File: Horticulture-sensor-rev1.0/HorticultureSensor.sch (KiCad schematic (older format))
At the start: 24 parts, among them J1 Conn_01x04, J2 Conn_02x05_Odd_Even, J3 Conn_01x03, J4 Conn_01x04, J5 Conn_01x03, J6 Conn_01x02, J7 Conn_01x02, J8 Conn_01x02, Q1 IRLML2030TRPBF, Q2 IRLML2030TRPBF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

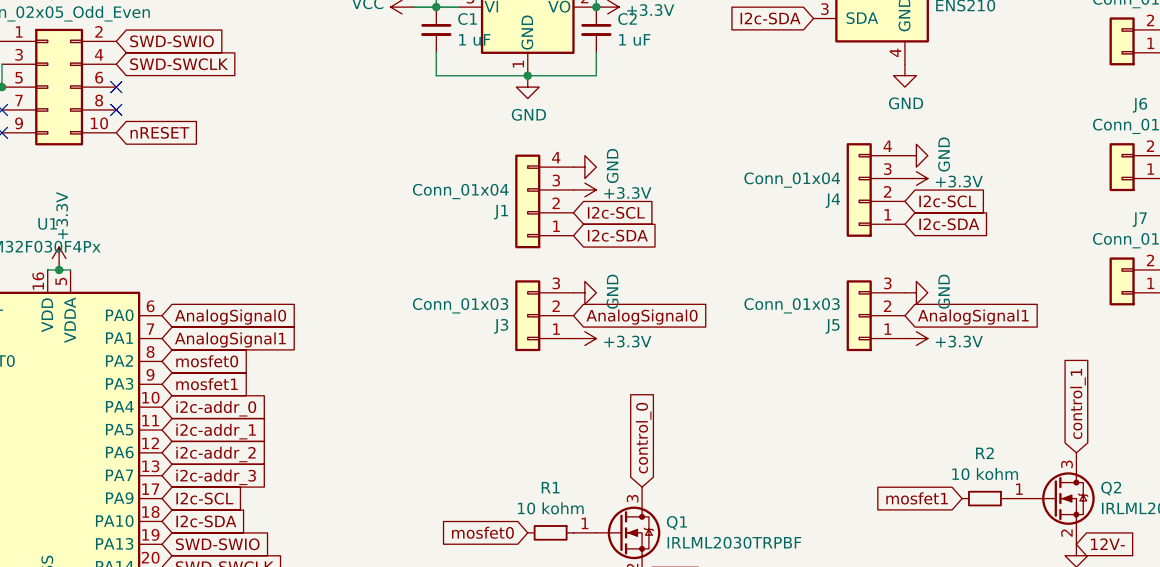
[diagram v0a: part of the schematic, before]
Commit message: Sensor board v1 complete
Not including motor/stepper controller
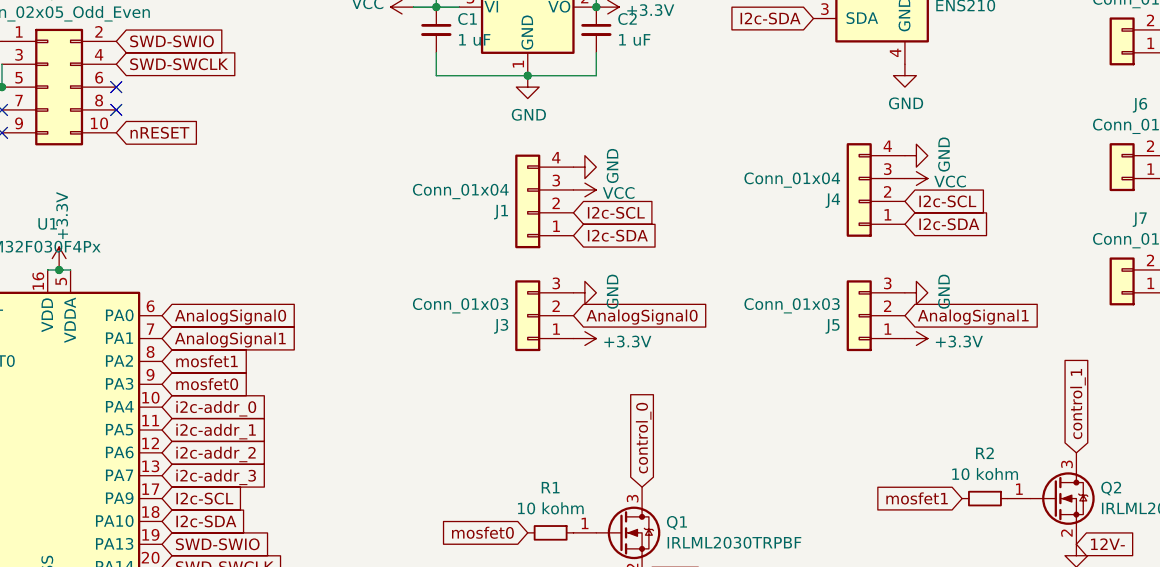
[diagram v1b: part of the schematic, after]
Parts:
- J1, J4: footprint Connector_Molex:Molex_PicoBlade_53261-0371_1x03-1MP_P1.25mm_Horizontal -> Connector_JST:JST_XH_S4B-XH-A-1_1x04_P2.50mm_Horizontal
- J3, J5: footprint Connector_Molex:Molex_PicoBlade_53047-0310_1x03_P1.25mm_Vertical -> Connector_JST:JST_XH_B3B-XH-A_1x03_P2.50mm_Vertical
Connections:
- net +3V3: no longer J1.3 (Pin_3), J4.3 (Pin_3)
- net VCC: now also J1.3 (Pin_3), J4.3 (Pin_3)
- net mosfet0: now also U1.9 (PA3); no longer U1.8 (PA2)
- net mosfet1: now also U1.8 (PA2); no longer U1.9 (PA3)
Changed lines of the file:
@@
 F 0 "J3" H 10330 7192 50  0000 L CNN
 F 1 "Conn_01x03" H 10330 7101 50  0000 L CNN
-F 2 "Connector_Molex:Molex_PicoBlade_53047-0310_1x03_P1.25mm_Vertical" H 10250 7150 50  0001 C CNN
+F 2 "Connector_JST:JST_XH_B3B-XH-A_1x03_P2.50mm_Vertical" H 10250 7150 50  0001 C CNN
 F 3 "~" H 10250 7150 50  0001 C CNN
 	1    10250 7150
@@
 F 0 "J1" H 10330 6692 50  0000 L CNN
 F 1 "Conn_01x04" H 10330 6601 50  0000 L CNN
-F 2 "Connector_Molex:Molex_PicoBlade_53261-0371_1x03-1MP_P1.25mm_Horizontal" H 10250 6700 50  0001 C CNN
+F 2 "Connector_JST:JST_XH_S4B-XH-A-1_1x04_P2.50mm_Horizontal" H 10250 6700 50  0001 C CNN
 F 3 "~" H 10250 6700 50  0001 C CNN
 	1    10250 6700
@@
 Text GLabel 8650 7550 2    50   Input ~ 0
 i2c-addr_0
-Text GLabel 8650 7450 2    50   Input ~ 0
+Text GLabel 8650 7350 2    50   Input ~ 0
 mosfet1
 Text GLabel 10350 8750 0    50   Input ~ 0
@@
 Text GLabel 8650 7150 2    50   Input ~ 0
 AnalogSignal0
-Text GLabel 8650 7350 2    50   Input ~ 0
+Text GLabel 8650 7450 2    50   Input ~ 0
 mosfet0
 $Comp
@@
 F 0 "J4" H 11780 6642 50  0000 L CNN
 F 1 "Conn_01x04" H 11780 6551 50  0000 L CNN
-F 2 "Connector_Molex:Molex_PicoBlade_53261-0371_1x03-1MP_P1.25mm_Horizontal" H 11700 6650 50  0001 C CNN
+F 2 "Connector_JST:JST_XH_S4B-XH-A-1_1x04_P2.50mm_Horizontal" H 11700 6650 50  0001 C CNN
 F 3 "~" H 11700 6650 50  0001 C CNN
 	1    11700 6650
@@
 F 0 "J5" H 11780 7192 50  0000 L CNN
 F 1 "Conn_01x03" H 11780 7101 50  0000 L CNN
-F 2 "Connector_Molex:Molex_PicoBlade_53047-0310_1x03_P1.25mm_Vertical" H 11700 7150 50  0001 C CNN
+F 2 "Connector_JST:JST_XH_B3B-XH-A_1x03_P2.50mm_Vertical" H 11700 7150 50  0001 C CNN
 F 3 "~" H 11700 7150 50  0001 C CNN
 	1    11700 7150
@@
 NoConn ~ 7650 8250
 $Comp
-L power:+3.3V #PWR0105
-U 1 1 5F355D47
-P 10450 6600
-F 0 "#PWR0105" H 10450 6450 50  0001 C CNN
-F 1 "+3.3V" V 10465 6728 50  0000 L CNN
-F 2 "" H 10450 6600 50  0001 C CNN
-F 3 "" H 10450 6600 50  0001 C CNN
-	1    10450 6600
-	0    1    1    0
-$EndComp
-$Comp
-L power:+3.3V #PWR0116
-U 1 1 5F355FAD
-P 11900 6550
-F 0 "#PWR0116" H 11900 6400 50  0001 C CNN
-F 1 "+3.3V" V 11915 6678 50  0000 L CNN
-F 2 "" H 11900 6550 50  0001 C CNN
-F 3 "" H 11900 6550 50  0001 C CNN
-	1    11900 6550
-	0    1    1    0
-$EndComp
-$Comp
 L Connector_Generic:Conn_01x02 J8
 U 1 1 5F35653E
@@
 Wire Wire Line
 	9750 5800 9850 5800
+$Comp
+L power:VCC #PWR0105
+U 1 1 5F38DC6C
+P 10450 6600
+F 0 "#PWR0105" H 10450 6450 50  0001 C CNN
+F 1 "VCC" V 10465 6728 50  0000 L CNN
+F 2 "" H 10450 6600 50  0001 C CNN
+F 3 "" H 10450 6600 50  0001 C CNN
+	1    10450 6600
+	0    1    1    0
+$EndComp
+$Comp
+L power:VCC #PWR0116
+U 1 1 5F38E28F
+P 11900 6550
+F 0 "#PWR0116" H 11900 6400 50  0001 C CNN
+F 1 "VCC" V 11915 6678 50  0000 L CNN
+F 2 "" H 11900 6550 50  0001 C CNN
+F 3 "" H 11900 6550 50  0001 C CNN
+	1    11900 6550
+	0    1    1    0
+$EndComp
 $EndSCHEMATC

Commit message: Somethings updated
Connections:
- net GND: now also R1.2, R2.2
- net mosfet0: now also Q1.1 (G), R1.1; no longer R1.2
- net mosfet1: now also Q2.1 (G), R2.1; no longer R2.2
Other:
- moved on the sheet: R1, R2
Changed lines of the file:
@@
 L Device:R_Small R2
 U 1 1 5F2107E9
-P 12250 7950
-F 0 "R2" V 12054 7950 50  0000 C CNN
-F 1 "10 kohm" V 12145 7950 50  0000 C CNN
-F 2 "Resistor_SMD:R_0805_2012Metric" H 12250 7950 50  0001 C CNN
-F 3 "~" H 12250 7950 50  0001 C CNN
-	1    12250 7950
-	0    1    1    0
+P 12350 8050
+F 0 "R2" V 12154 8050 50  0000 C CNN
+F 1 "10 kohm" V 12245 8050 50  0000 C CNN
+F 2 "Resistor_SMD:R_0805_2012Metric" H 12350 8050 50  0001 C CNN
+F 3 "~" H 12350 8050 50  0001 C CNN
+	1    12350 8050
+	1    0    0    -1
 $EndComp
 $Comp
 L Device:R_Small R1
 U 1 1 5F211AEC
-P 10350 8100
-F 0 "R1" V 10154 8100 50  0000 C CNN
-F 1 "10 kohm" V 10245 8100 50  0000 C CNN
-F 2 "Resistor_SMD:R_0805_2012Metric" H 10350 8100 50  0001 C CNN
-F 3 "~" H 10350 8100 50  0001 C CNN
-	1    10350 8100
-	0    1    1    0
+P 10450 8200
+F 0 "R1" V 10254 8200 50  0000 C CNN
+F 1 "10 kohm" V 10345 8200 50  0000 C CNN
+F 2 "Resistor_SMD:R_0805_2012Metric" H 10450 8200 50  0001 C CNN
+F 3 "~" H 10450 8200 50  0001 C CNN
+	1    10450 8200
+	1    0    0    -1
 $EndComp
 $Comp
@@
 	0    1    1    0
 $EndComp
+Wire Wire Line
+	10250 8100 10450 8100
+Connection ~ 10450 8100
+Wire Wire Line
+	10750 8300 10450 8300
+Connection ~ 10750 8300
+Wire Wire Line
+	12150 7950 12350 7950
+Connection ~ 12350 7950
+Wire Wire Line
+	12350 8150 12650 8150
+Connection ~ 12650 8150
 $EndSCHEMATC
